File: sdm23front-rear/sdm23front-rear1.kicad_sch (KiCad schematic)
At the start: 19 parts

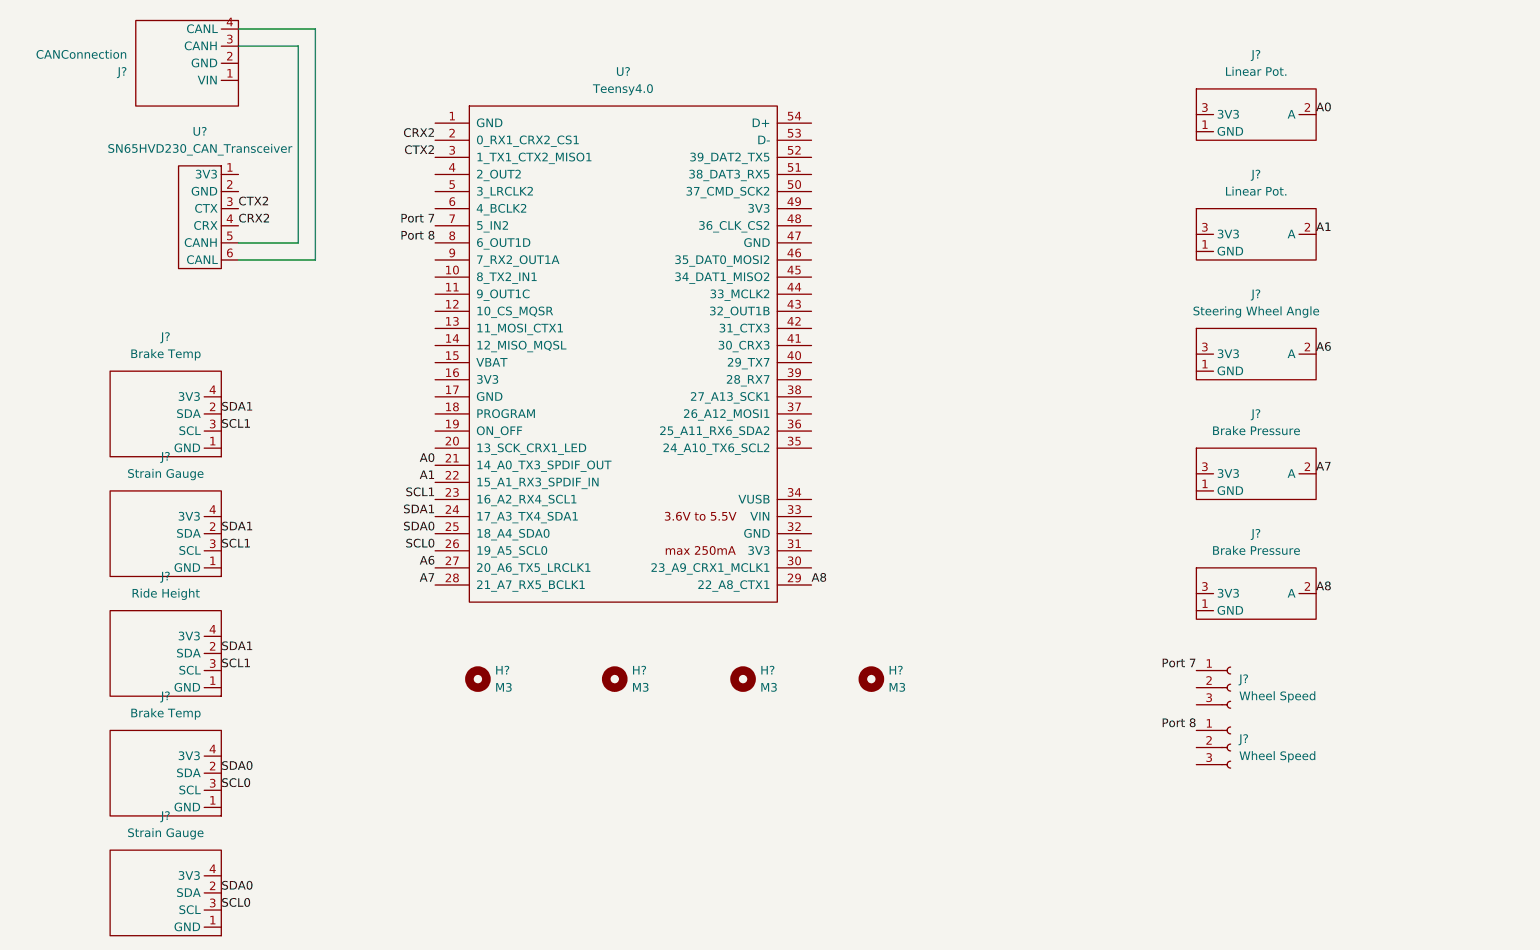
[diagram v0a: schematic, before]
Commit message: Updated CAN Transceiver symbol
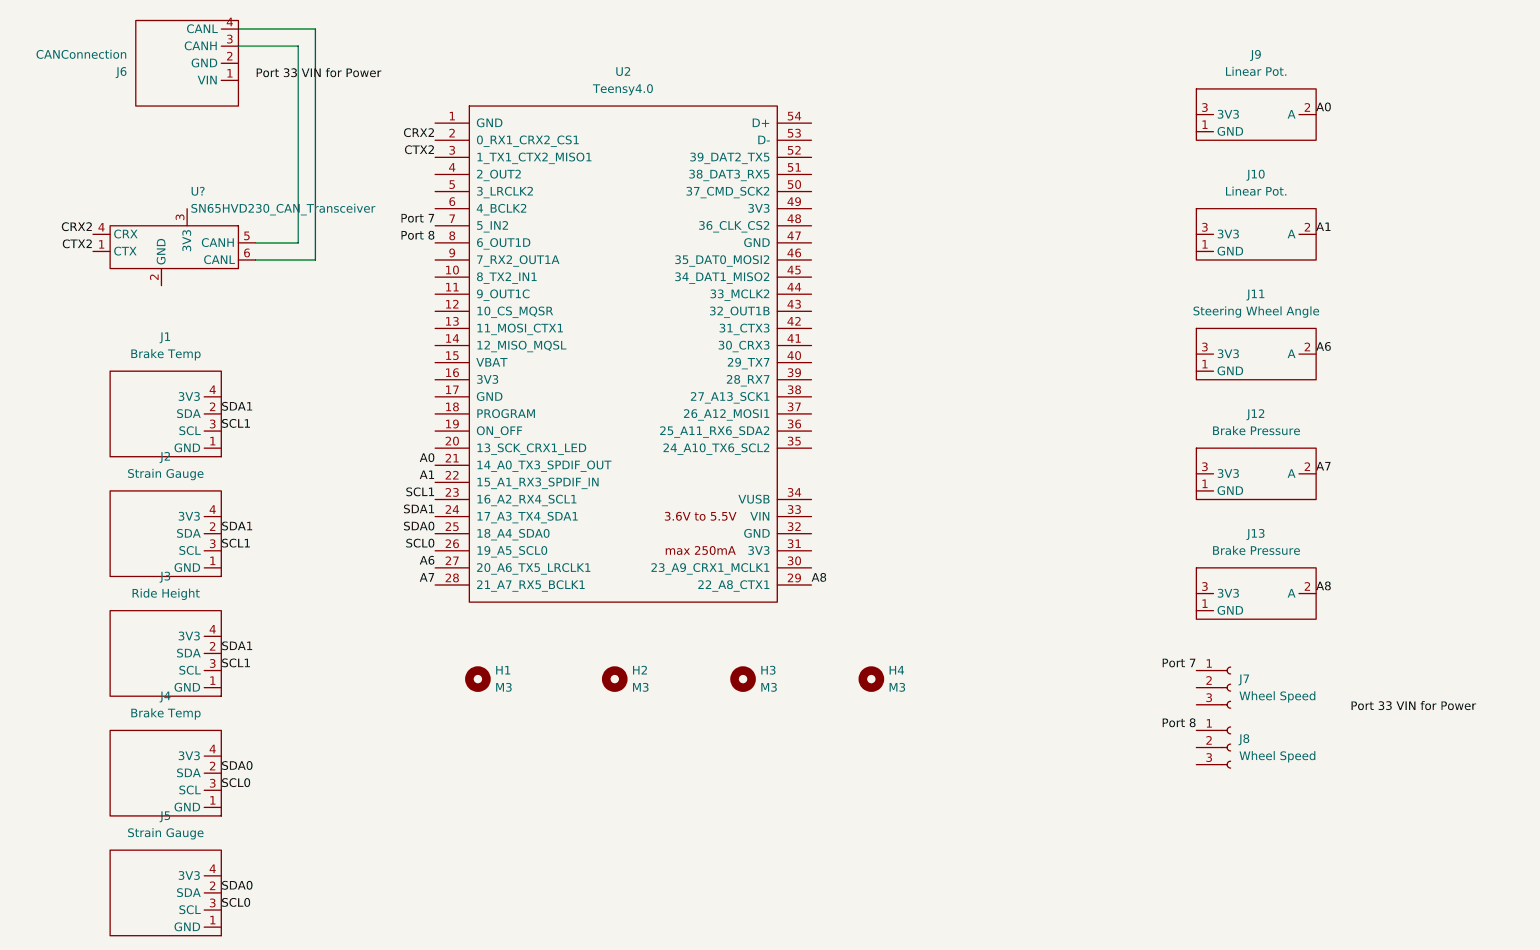
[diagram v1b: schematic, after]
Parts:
- removed U?: SN65HVD230_CAN_Transceiver, symbol sdm:SN65HVD230_CAN_Transceiver
- added U?: SN65HVD230_CAN_Transceiver, symbol sdm:SN65HVD230_CAN_Transceiver
- H1, H2, H3, H4: renamed from H?; footprint (none) -> MountingHole:MountingHole_3.2mm_M3
- J1, J2, J3, J4, J5, J6: renamed from J?; footprint (none) -> TerminalBlock_TE-Connectivity:TerminalBlock_TE_282834-4_1x04_P2.54mm_Horizontal
- gave numbers to parts that had none: 8
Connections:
- net CRX2: now also U?.4 (CRX)
- net CTX2: now also U?.1 (CTX)
- net at J6.3 (CANH): now also U?.5 (CANH)
- net at J6.4 (CANL): now also U?.6 (CANL)
